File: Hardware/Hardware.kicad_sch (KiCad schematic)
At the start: 23 parts, among them J1 Conn_01x04, SW1 SW_Push, U1 STM32WB55RGVx, Y1 32kHz768, Y2 32MHz

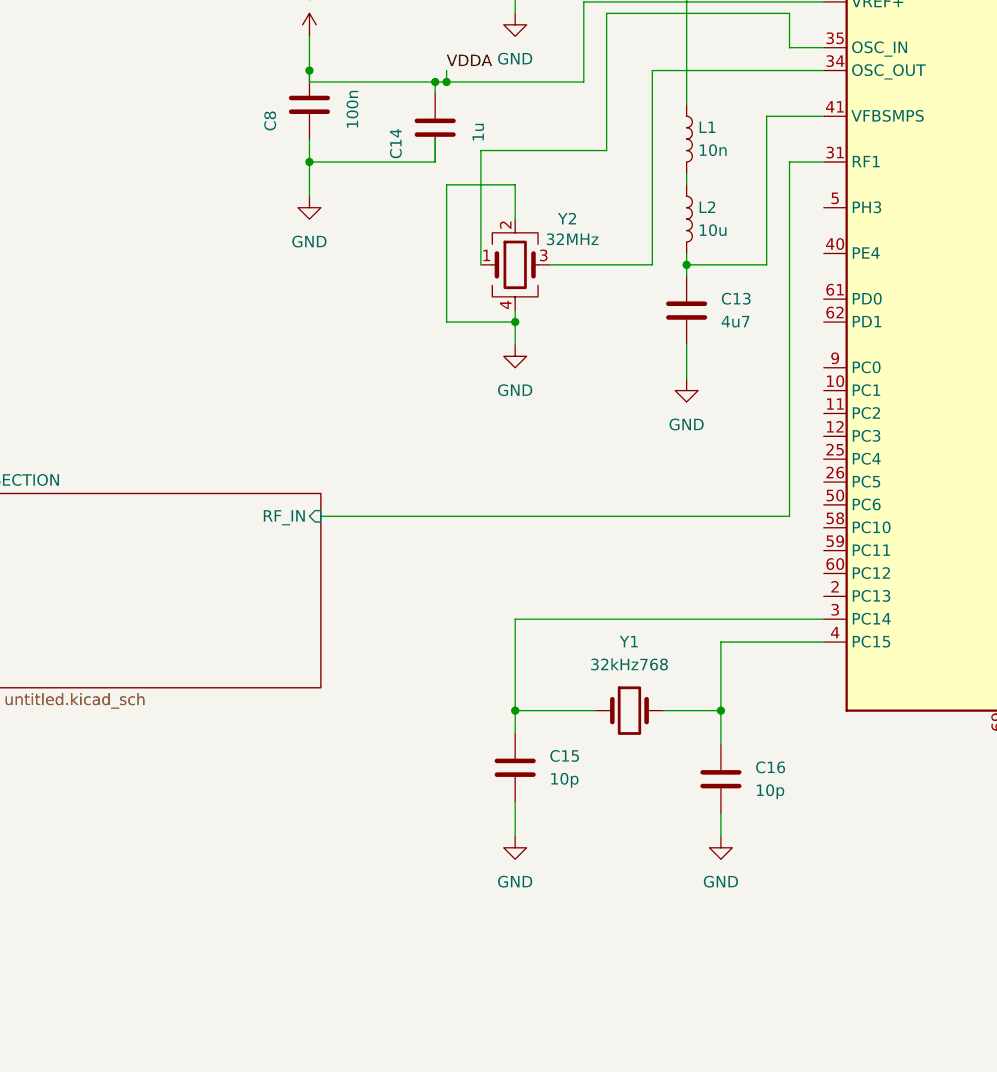
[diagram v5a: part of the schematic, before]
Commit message: [BOOT] : Pour que la carte fonctionne bien, on met une résistance pull down à PH3_BOOT, ce qui permet au microcontroleur de continuer son execution normalement
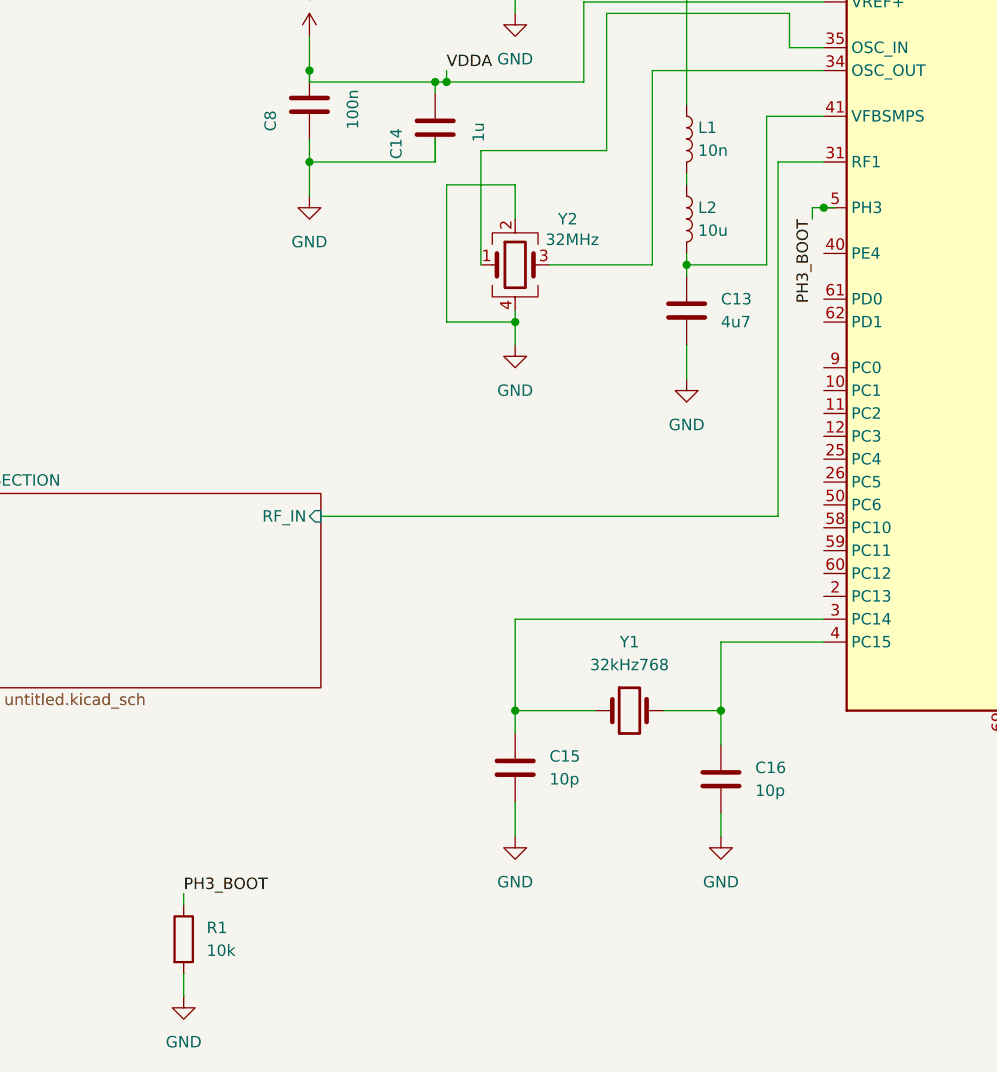
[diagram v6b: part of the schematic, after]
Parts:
- added R1: 10k, symbol Device:R
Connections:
- net GND: now also R1.2
- net PH3_BOOT: now reaches U1.5 (PH3)
- net PH3_BOOT: now also R1.1
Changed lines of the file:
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@@
+	)
+	(junction
+		(at 119.38 76.2)
+		(diameter 0)
+		(color 0 0 0 0)
 	)
 	(junction
@@
 	(wire
 		(pts
-			(xy 115.57 110.49) (xy 115.57 71.12)
+			(xy 114.3 110.49) (xy 114.3 71.12)
 		)
 		(stroke
@@
 	(wire
 		(pts
+			(xy 118.11 76.2) (xy 119.38 76.2)
+		)
+		(stroke
+			(width 0)
+			(type default)
+		)
+	)
+	(wire
+		(pts
 			(xy 104.14 72.39) (xy 104.14 73.66)
 		)
@@
 	(wire
 		(pts
+			(xy 48.26 161.29) (xy 48.26 163.83)
+		)
+		(stroke
+			(width 0)
+			(type default)
+		)
+	)
+	(wire
+		(pts
 			(xy 167.64 81.28) (xy 165.1 81.28)
 		)
@@
 	(wire
 		(pts
+			(xy 119.38 76.2) (xy 120.65 76.2)
+		)
+		(stroke
+			(width 0)
+			(type default)
+		)
+	)
+	(wire
+		(pts
 			(xy 81.28 31.75) (xy 90.17 31.75)
 		)
@@
 	(wire
 		(pts
+			(xy 48.26 152.4) (xy 48.26 153.67)
+		)
+		(stroke
+			(width 0)
+			(type default)
+		)
+	)
+	(wire
+		(pts
 			(xy 119.38 124.46) (xy 107.95 124.46)
 		)
@@
 	(wire
 		(pts
-			(xy 63.5 110.49) (xy 115.57 110.49)
+			(xy 63.5 110.49) (xy 114.3 110.49)
 		)
 		(stroke
@@
 	(wire
 		(pts
-			(xy 119.38 71.12) (xy 115.57 71.12)
+			(xy 119.38 71.12) (xy 114.3 71.12)
 		)
 		(stroke
@@
 		(pts
 			(xy 115.57 54.61) (xy 115.57 58.42)
+		)
+		(stroke
+			(width 0)
+			(type default)
+		)
+	)
+	(wire
+		(pts
+			(xy 118.11 77.47) (xy 118.11 76.2)
 		)
 		(stroke
@@
 			)
 			(justify left bottom)
+		)
+	)
+	(label "PH3_BOOT"
+		(at 48.26 152.4 0)
+		(effects
+			(font
+				(size 1.27 1.27)
+			)
+			(justify left bottom)
+		)
+	)
+	(label "PH3_BOOT"
+		(at 118.11 77.47 270)
+		(effects
+			(font
+				(size 1.27 1.27)
+			)
+			(justify right bottom)
 		)
 	)
@@
 	(symbol
 		(lib_id "power:GND")
+		(at 48.26 163.83 0)
+		(unit 1)
+		(exclude_from_sim no)
+		(in_bom yes)
+		(on_board yes)
+		(dnp no)
+		(fields_autoplaced yes)
+		(property "Reference" "#PWR025"
+			(at 48.26 170.18 0)
+			(effects
+				(font
+					(size 1.27 1.27)
+				)
+				(hide yes)
+			)
+		)
+		(property "Value" "GND"
+			(at 48.26 168.91 0)
+			(effects
+				(font
+					(size 1.27 1.27)
+				)
+			)
+		)
+		(property "Footprint" ""
+			(at 48.26 163.83 0)
+			(effects
+				(font
+					(size 1.27 1.27)
+				)
+				(hide yes)
+			)
+		)
+		(property "Datasheet" ""
+			(at 48.26 163.83 0)
+			(effects
+				(font
+					(size 1.27 1.27)
+				)
+				(hide yes)
+			)
+		)
+		(property "Description" "Power symbol creates a global label with name \"GND\" , ground"
+			(at 48.26 163.83 0)
+			(effects
+				(font
+					(size 1.27 1.27)
+				)
+				(hide yes)
+			)
+		)
+		(pin "1"
+		)
+		(instances
+			(project ""
+				(path "/ba4846b8-7c71-441f-b11b-b34cbea60d05"
+					(reference "#PWR025")
+					(unit 1)
+				)
+			)
+		)
+	)
+	(symbol
+		(lib_id "power:GND")
 		(at 142.24 137.16 0)
 		(unit 1)
@@
 					(unit 1)
 				)
+			)
+		)
+	)
+	(symbol
+		(lib_id "Device:R")
+		(at 48.26 157.48 0)
+		(unit 1)
+		(exclude_from_sim no)
+		(in_bom yes)
+		(on_board yes)
+		(dnp no)
+		(fields_autoplaced yes)
+		(property "Reference" "R1"
+			(at 50.8 156.2099 0)
+			(effects
+				(font
+					(size 1.27 1.27)
+				)
+				(justify left)
+			)
+		)
+		(property "Value" "10k"
+			(at 50.8 158.7499 0)
+			(effects
+				(font
+					(size 1.27 1.27)
+				)
+				(justify left)
+			)
+		)
+		(property "Footprint" ""
+			(at 46.482 157.48 90)
+			(effects
+				(font
+					(size 1.27 1.27)
+				)
+				(hide yes)
+			)
+		)
+		(property "Datasheet" "~"
+			(at 48.26 157.48 0)
+			(effects
+				(font
+					(size 1.27 1.27)
+				)
+				(hide yes)
+			)
+		)
+		(property "Description" "Resistor"
+			(at 48.26 157.48 0)
+			(effects
+				(font
+					(size 1.27 1.27)
+				)
+				(hide yes)
+			)
+		)
+		(pin "1"
+		)
+		(pin "2"
+		)
+		(instances
+			(project ""
+				(path "/ba4846b8-7c71-441f-b11b-b34cbea60d05"
+					(reference "R1")
+					(unit 1)
+				)

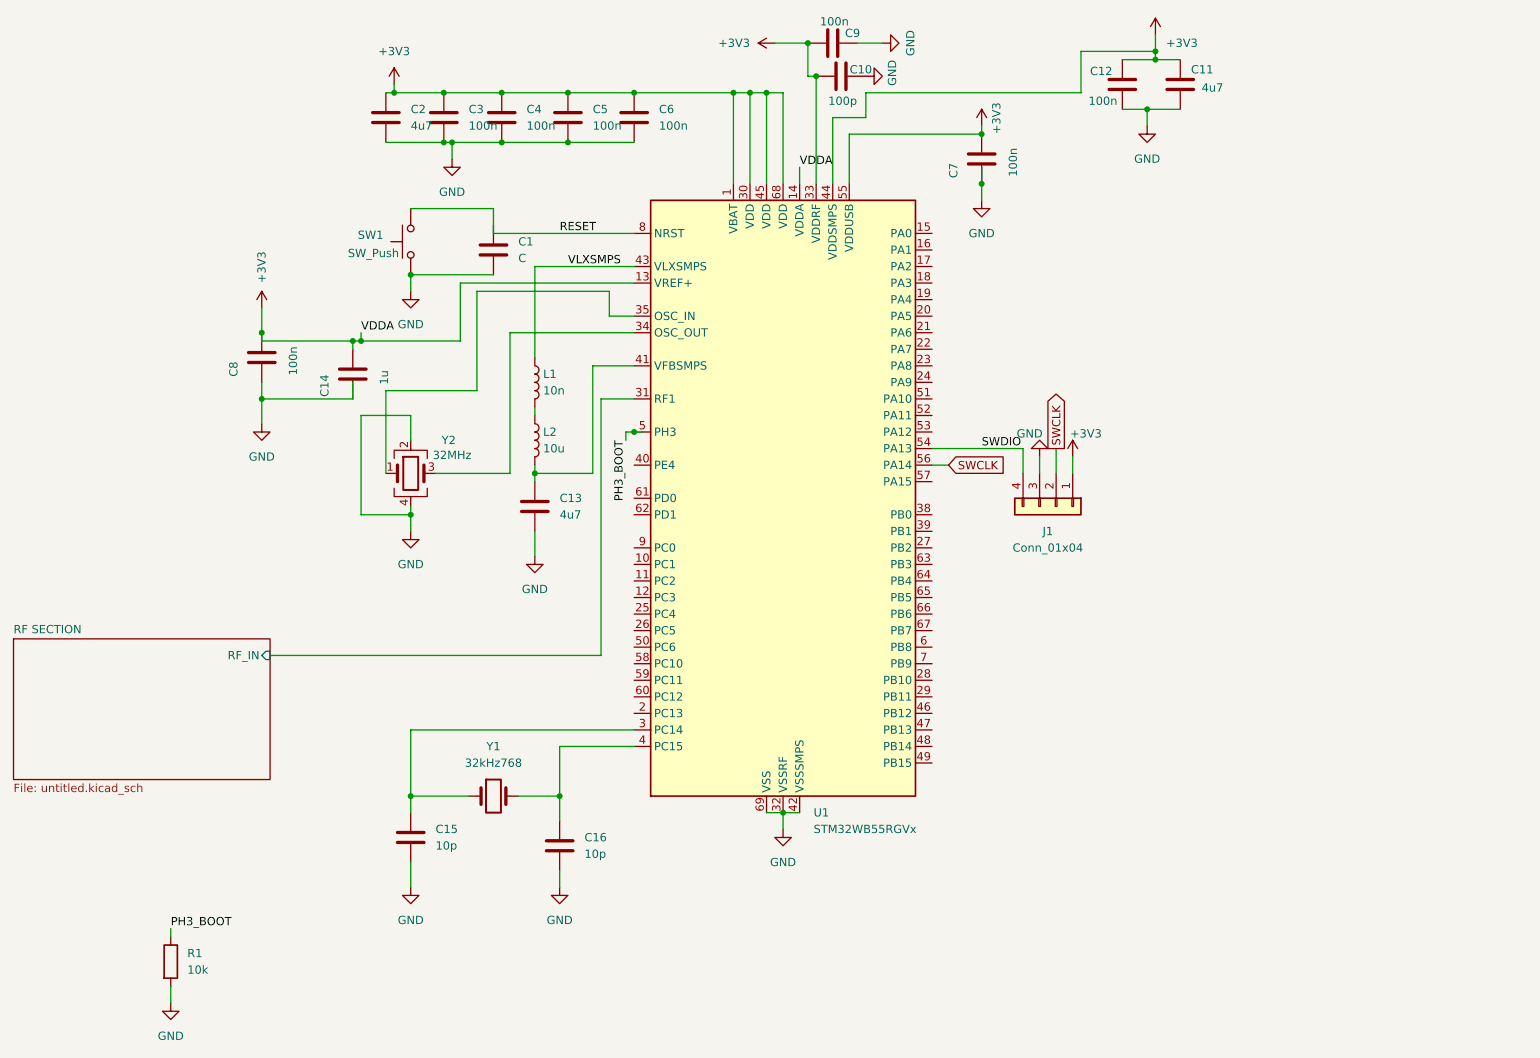
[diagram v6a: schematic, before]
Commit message: [Hierachisation] hierachisation de la schématique et ajout de l'USB
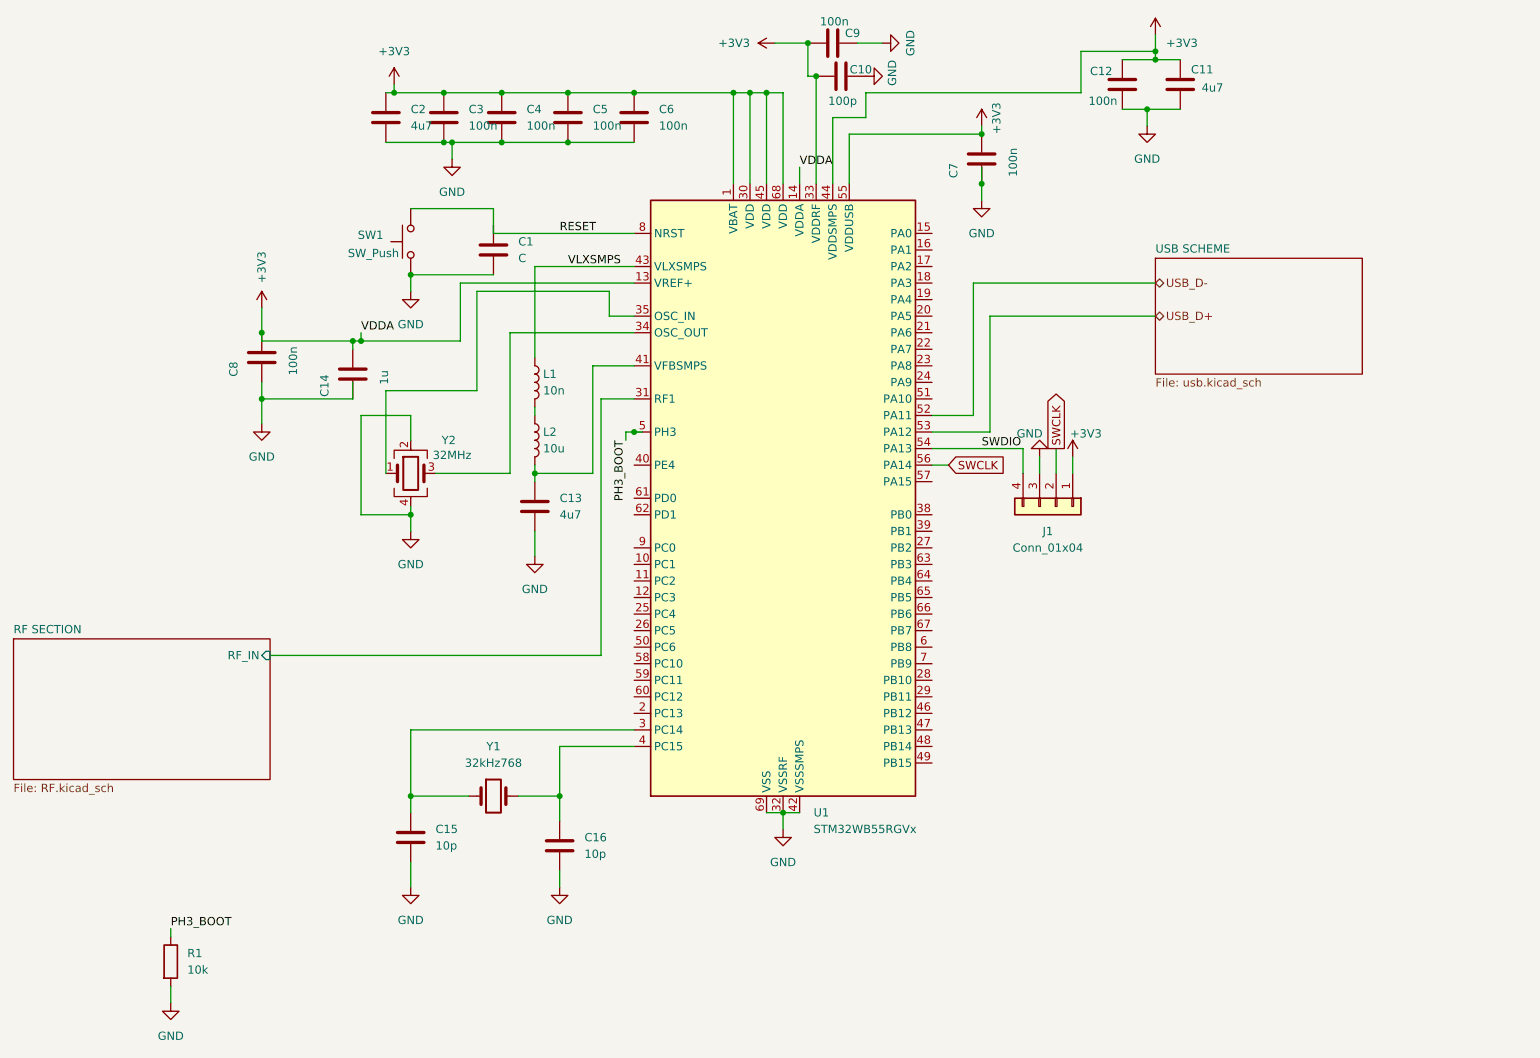
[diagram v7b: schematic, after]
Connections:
- net USB_D-: now reaches U1.52 (PA11)
- net USB_D+: now reaches U1.53 (PA12)
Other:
- added sheet USB SCHEME (usb.kicad_sch)
- sheet RF SECTION: file untitled.kicad_sch -> RF.kicad_sch
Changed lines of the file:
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@@
 	(wire
 		(pts
+			(xy 171.45 53.34) (xy 199.39 53.34)
+		)
+		(stroke
+			(width 0)
+			(type default)
+		)
+	)
+	(wire
+		(pts
 			(xy 152.4 30.48) (xy 172.72 30.48)
 		)
@@
 	(wire
 		(pts
+			(xy 173.99 58.42) (xy 199.39 58.42)
+		)
+		(stroke
+			(width 0)
+			(type default)
+		)
+	)
+	(wire
+		(pts
 			(xy 107.95 143.51) (xy 107.95 146.05)
 		)
@@
 	(wire
 		(pts
+			(xy 165.1 73.66) (xy 171.45 73.66)
+		)
+		(stroke
+			(width 0)
+			(type default)
+		)
+	)
+	(wire
+		(pts
 			(xy 85.09 77.47) (xy 85.09 73.66)
 		)
@@
 	(wire
 		(pts
+			(xy 171.45 73.66) (xy 171.45 53.34)
+		)
+		(stroke
+			(width 0)
+			(type default)
+		)
+	)
+	(wire
+		(pts
 			(xy 113.03 66.04) (xy 113.03 82.55)
 		)
@@
 	(wire
 		(pts
+			(xy 173.99 76.2) (xy 173.99 58.42)
+		)
+		(stroke
+			(width 0)
+			(type default)
+		)
+	)
+	(wire
+		(pts
 			(xy 81.28 31.75) (xy 90.17 31.75)
 		)
@@
 	(wire
 		(pts
+			(xy 165.1 76.2) (xy 173.99 76.2)
+		)
+		(stroke
+			(width 0)
+			(type default)
+		)
+	)
+	(wire
+		(pts
 			(xy 93.98 132.08) (xy 85.09 132.08)
 		)
@@
 		)
 	)
+	(hierarchical_label "USB_D+"
+		(shape bidirectional)
+		(at 199.39 58.42 0)
+		(effects
+			(font
+				(size 1.27 1.27)
+			)
+			(justify left)
+		)
+	)
+	(hierarchical_label "USB_D-"
+		(shape bidirectional)
+		(at 199.39 53.34 0)
+		(effects
+			(font
+				(size 1.27 1.27)
+			)
+			(justify left)
+		)
+	)
 	(symbol
 		(lib_id "power:GND")
@@
 			)
 		)
-		(property "Sheetfile" "untitled.kicad_sch"
+		(property "Sheetfile" "RF.kicad_sch"
 			(at 24.13 130.1246 0)
 			(effects
@@
 				)
 			)
+		)
+	)
+	(sheet
+		(at 199.39 49.53)
+		(size 31.75 17.78)
+		(exclude_from_sim no)
+		(in_bom yes)
+		(on_board yes)
+		(dnp no)
+		(fields_autoplaced yes)
+		(stroke
+			(width 0.1524)
+			(type solid)
+		)
+		(fill
+			(color 0 0 0 0.0000)
+		)
+		(property "Sheetname" "USB SCHEME"
+			(at 199.39 48.8184 0)
+			(effects
+				(font
+					(size 1.27 1.27)
+				)
+				(justify left bottom)
+			)
+		)
+		(property "Sheetfile" "usb.kicad_sch"
+			(at 199.39 67.8946 0)
+			(effects
+				(font
+					(size 1.27 1.27)
+				)
+				(justify left top)
+			)
+		)
+		(instances
+			(project "Hardware"
+				(path "/ba4846b8-7c71-441f-b11b-b34cbea60d05"
+					(page "3")
+				)
+			)
